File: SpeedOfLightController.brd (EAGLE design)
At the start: 99.7 x 100 mm, 140 parts, among them IC10 74LS595D, IC11 74LS595D, Q10 FDN360P, Q12 FDN360P, Q14 FDN360P, Q16 FDN360P, Q18 FDN360P, Q20 FDN360P, Q22 FDN360P, Q24 FDN360P, Q26 FDN360P, SW2 MOMENTARYBUTTON, U1 ATMEGA328PBTQFP-32, U2 LM380NDIP14, U3 AD5111ADLFCSP10, X1 JST-XH-08-PIN-LONG-PAD, X10 JST-XH-06-PIN-LONG-PAD, X11 JST-XH-06-PIN-LONG-PAD, X12 JST-XH-06-PIN-LONG-PAD, X13 JST-XH-06-PIN-LONG-PAD, X14 JST-XH-07-PIN-LONG-PAD, X15 JST-XH-02-PIN-LONG-PAD, X16 JST-XH-02-PIN-LONG-PAD, X17 JST-XH-02-PIN-LONG-PAD, X18 JST-XH-02-PIN-LONG-PAD, X19 JST-XH-03-PIN-LONG-PAD, X2 JST-XH-08-PIN-LONG-PAD, X20 JST-XH-03-PIN-LONG-PAD, X21 JST-XH-03-PIN-LONG-PAD, X22 JST-XH-03-PIN-LONG-PAD, X3 JST-XH-08-PIN-LONG-PAD, X4 JST-XH-08-PIN-LONG-PAD, X5 JST-XH-08-PIN-LONG-PAD, X6 JST-XH-08-PIN-LONG-PAD, X7 JST-XH-08-PIN-LONG-PAD, X8 JST-XH-08-PIN-LONG-PAD, X9 JST-XH-08-PIN-LONG-PAD

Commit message: USBPD design review
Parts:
- removed CN1: (no value), adafruit:USB-MINIB
- removed F3: FIDUCIAL, ECE388:FIDUCIAL_1MM
- removed IC10, IC11: 74LS595D, 74xx-us:SO16
- removed JP13: (no value), pinhead:1X05
- removed JP14: (no value), pinhead:1X03
- removed R5: 82K, rcl:R0805
- removed SW2: MOMENTARYBUTTON, ECE388:SPST_NO_SMD
- removed X27: (no value), ECE388:W237-102
- added C14, C15: 0.1uF, rcl:C0805
- added C16: 680uF, rcl:140CLH-0810
- added C17: 220uF, rcl:140CLH-0810
- added H1, H2: MOUNT-HOLE3.0, holes:3,0
- added IC1, IC2: 74LS595D, 74xx-us:SO16
- added IC3: (no value), linear:TO263-5
- added J1: 6_PIN_SERIAL_CABLEPTH, SparkFun-Connectors:FTDI_BASIC
- added JP10: (no value), pinhead:1X03
- added JP2: JUMPER-SMT_3_1-NC_TRACE_SILK, SparkFun-Jumpers:SMT-JUMPER_3_1-NC_TRACE_SILK
- added JP5: (no value), pinhead:1X05
- added JP6: (no value), pinhead:1X04
- added JP7, JP8, JP9: (no value), pinhead:1X01
- added R59, R62: 1K5, rcl:R0805
- added R60, R63: 470, rcl:R0805
- added R61: 10K, rcl:R0805
- added SJ1, SJ3: (no value), ECE388:SJ
- added SJ4, SJ5: (no value), jumper:SJ_2W
- added SW1: MOMENTARYBUTTON, ECE388:SPST_NO_SMD
- added U4: AD5141ADLFCSP3, tmc:QFN50P300X300X80-17T160N
- added X25: JST-XH-03-PIN-LONG-PAD, Rembrandt Electronics - JST XH Connectors v1-0:JST-XH-03-PACKAGE-LONG-PAD
- C1, C4: value (none) -> 0.1uF
- C10, C12: value (none) -> 470uF; device rcl:C0805 -> rcl:140CLH-0810
- C11: value (none) -> 47uF
- C13: value (none) -> 4.7uF
- C2, C3: value (none) -> 22pF
- C7: value 22uF -> 0.1uF
- C8: value 22uF -> 47nF
- C9: value (none) -> 47nF
- F1: value (none) -> FIDUCIAL; device adafruit:1812 -> ECE388:FIDUCIAL_1MM
- JP1: value (none) -> JUMPER-SMT_3_1-NC_TRACE_SILK; device pinhead:2X03 -> SparkFun-Jumpers:SMT-JUMPER_3_1-NC_TRACE_SILK
- Q1: value (none) -> 16MHz
- Q10, Q14, Q16, Q20, Q22, Q24, Q26: value FDN360P -> AO3414SOT23; device transistor-power:SUPER-SOT3 -> tmc:SOT95P240X110-3N
- Q11, Q13, Q17, Q19, Q5, Q6, Q7: value (none) -> AO3415; device adafruit:SOT23 -> tmc:SOT95P240X110-3N
- Q12, Q18: value FDN360P -> AO3415; device transistor-power:SUPER-SOT3 -> tmc:SOT95P240X110-3N
- Q15, Q2, Q21, Q23, Q25, Q3, Q4, Q8, Q9: value (none) -> AO3414SOT23; device adafruit:SOT23 -> tmc:SOT95P240X110-3N
- R11, R17, R23, R29, R35, R41, R49, R51, R55: value 1K -> 10K
- R14, R20, R26, R32, R38, R44, R46, R54, R8: value 10K -> 1K
- R57: value 10K -> 0; device rcl:R0805 -> rcl:R0805W
- R6: value 4.3K -> 10K
- SJ2: device jumper:SJ_2 -> jumper:SJ_2W
- U$1: value MT3608SOT23-6 -> USBMICRO; device tmc:SOT95P280X110-6N -> tmc:USBMICRO
- U3: value AD5111ADLFCSP10 -> SSM2305ADMSOP8_2; device tmc:SON50P200X200X80-9T100X160N -> tmc:SOP65P490X95-8N
- X1, X2, X4, X5: value JST-XH-08-PIN-LONG-PAD -> JST-XH-06-PIN-LONG-PAD; device Rembrandt Electronics - JST XH Connectors v1-0:JST-XH-08-PACKAGE-LONG-PAD -> Rembrandt Electronics - JST XH Connectors v1-0:JST-XH-06-PACKAGE-LONG-PAD
- X10, X11, X12, X13: value JST-XH-06-PIN-LONG-PAD -> JST-XH-08-PIN-LONG-PAD; device Rembrandt Electronics - JST XH Connectors v1-0:JST-XH-06-PACKAGE-LONG-PAD -> Rembrandt Electronics - JST XH Connectors v1-0:JST-XH-08-PACKAGE-LONG-PAD
- X14: value JST-XH-07-PIN-LONG-PAD -> JST-XH-08-PIN-LONG-PAD; device Rembrandt Electronics - JST XH Connectors v1-0:JST-XH-07-PACKAGE-LONG-PAD -> Rembrandt Electronics - JST XH Connectors v1-0:JST-XH-08-PACKAGE-LONG-PAD
- X15, X16, X17: value JST-XH-02-PIN-LONG-PAD -> (none); device Rembrandt Electronics - JST XH Connectors v1-0:JST-XH-02-PACKAGE-LONG-PAD -> ECE388:W237-102
- X19, X20, X21: value JST-XH-03-PIN-LONG-PAD -> JST-XH-02-PIN-LONG-PAD; device Rembrandt Electronics - JST XH Connectors v1-0:JST-XH-03-PACKAGE-LONG-PAD -> Rembrandt Electronics - JST XH Connectors v1-0:JST-XH-02-PACKAGE-LONG-PAD
- X23, X24: value (none) -> JST-XH-03-PIN-LONG-PAD; device ECE388:W237-102 -> Rembrandt Electronics - JST XH Connectors v1-0:JST-XH-03-PACKAGE-LONG-PAD
- X3: value JST-XH-08-PIN-LONG-PAD -> JST-XH-07-PIN-LONG-PAD; device Rembrandt Electronics - JST XH Connectors v1-0:JST-XH-08-PACKAGE-LONG-PAD -> Rembrandt Electronics - JST XH Connectors v1-0:JST-XH-07-PACKAGE-LONG-PAD
- moved F1 130.6 mm to (99.1, 130.8)
- moved X11 91.0 mm to (60.3, 118.7), turned to 270 degrees
- moved X10 88.3 mm to (50.2, 118.7), turned to 270 degrees
- moved C7 87.3 mm to (69.2, 90.2), turned to 270 degrees
- moved U2 81.5 mm to (76.2, 59.7), turned to 180 degrees
- moved R3 80.1 mm to (74.3, 93.3), turned to 0 degrees
- moved C9 79.5 mm to (76.2, 65.4), turned to 180 degrees
- moved R21 78.1 mm to (80.0, 99.1)
- moved X13 76.5 mm to (80.6, 118.7), turned to 270 degrees
- moved X12 76.4 mm to (70.5, 118.7), turned to 270 degrees
- moved C10 75.5 mm to (75.6, 43.2), turned to 180 degrees
- moved R55 74.8 mm to (23.5, 87.6), turned to 270 degrees
- moved Q10 74.7 mm to (79.4, 103.5), turned to 90 degrees
- moved R24 73.6 mm to (77.5, 99.1)
- moved R9 73.5 mm to (69.8, 99.1), turned to 90 degrees
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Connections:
- removed net N$26: C11.2, X23.1
- removed net N$33: C7.1, D1.C, F1.1, R5.2
- removed net SOUND_C: R58.1, U1.3, U3.6
- removed net SOUND_UD: U1.22, U3.7
- new net ADSOUND+: SJ4.1, U3.5
- new net ADSOUND-: SJ5.3, U3.8
- new net D+: JP5.3, R58.1, R59.2, R60.2, U$1.P$3
- new net D-: JP5.2, R61.2, R62.1, R63.1, U$1.P$2
- new net FTDIRX: J1.TXO, JP1.2
- new net FTDITX: J1.RXI, JP2.2
- new net LMSOUND: C12.-, SJ4.3
- new net N$40: IC3.5, SJ2.2
- new net N$41: C17.+, IC3.4, L1.P$2, SJ3.2
- new net SOUND+: SJ4.2, X15.1
- new net SOUND-: SJ5.2, X16.2
- new net UCD+: R60.1, U1.6
- new net UCD-: R63.2, U1.3
- net +12V: now also C16.+, IC3.1, JP10.2, Q11.2, Q13.2, Q17.2, Q19.2, Q5.2, Q6.2, Q7.2, R13.2, R14.2, R15.2, R25.2, R26.2, R37.2, R38.2, SJ1.2, SJ2.3, X19.1, X19.2, X20.1, X20.2, X21.1, X21.2; no longer F1.2, JP14.2, Q10.2, Q14.2, Q16.2, Q20.2, Q22.2, Q24.2, Q26.2, R23.2, R31.2, R35.2, R43.2, R47.2, R51.2, R55.2, X15.1, X15.2, X16.1, X16.2, X17.2, X27.1
- net +5V: now also C10.+, C14.2, C15.1, C4.2, C6.1, C7.1, IC1.16, IC2.16, J1.VCC, JP10.1, R4.2, R6.2, R61.1, SJ3.1, U3.6, U4.10, U4.13, U4.16, U4.9, X3.1; no longer C1.1, C12.2, C2.1, C8.1, C9.1, CN1.VBUS, IC10.16, IC11.16, JP1.5, JP13.1, JP14.1, L1.P$1, R3.2, R57.2, SJ2.3, U$1.5, X14.1
- net A: now also Q20.3, X10.5, X11.5, X12.5, X13.5, X14.5; no longer Q4.3, X1.5, X2.5, X3.5, X4.5, X5.5
- net AN1: now also IC1.7, R7.1; no longer IC10.7, R21.1
- net AN2: now also IC2.15, R19.1; no longer IC11.15, R25.1
- net AN3: now also IC2.1, R31.1; no longer IC11.1, R29.1
- net AN4: now also IC2.2, R8.1; no longer IC11.2, R33.1
- net AN5: now also IC2.3, R20.1; no longer IC11.3, R37.1
- net AN6: now also IC2.4, R32.1; no longer IC11.4, R41.1
- net AN7: now also IC2.5, R9.1; no longer IC11.5, R45.1
- net AN8: now also IC2.6, R21.1; no longer IC11.6, R49.1
- net AN9: now also IC2.7, R33.1; no longer IC11.7, R53.1
- net B: now also Q21.3, X10.6, X11.6, X12.6, X13.6, X14.6; no longer Q2.3, X1.6, X2.6, X3.6, X4.6, X5.6
- net B_COL_0: now also X1.4, X2.4; no longer X10.4, X11.4
- net B_COL_1: now also X1.5, X2.5; no longer X10.5, X11.5
- net B_COL_2: now also X1.6, X2.6; no longer X10.6, X11.6
- net B_COL_3: now also X4.4, X5.4; no longer X12.4, X13.4
- net B_COL_4: now also X4.5, X5.5; no longer X12.5, X13.5
- net B_COL_5: now also X4.6, X5.6; no longer X12.6, X13.6
- net B_ROW_0: now also X1.1, X4.1; no longer X10.1, X12.1
- net B_ROW_1: now also X1.2, X4.2; no longer X10.2, X12.2
- net B_ROW_2: now also X1.3, X4.3; no longer X10.3, X12.3
- net B_ROW_3: now also X2.1, X5.1; no longer X11.1, X13.1
- net B_ROW_4: now also X2.2, X5.2; no longer X11.2, X13.2
- net B_ROW_5: now also X2.3, X5.3; no longer X11.3, X13.3
- net C: now also Q22.3, X10.7, X11.7, X12.7, X13.7, X14.7; no longer Q3.3, X1.7, X2.7, X3.7, X4.7, X5.7
- net D: now also Q23.3, X10.1, X11.1, X12.1, X13.1, X14.1; no longer Q5.3, X1.1, X2.1, X3.1, X4.1, X5.1
- net DTR: now also C1.2, J1.DTR; no longer C6.2, JP1.6
- net E: now also Q24.3, X10.2, X11.2, X12.2, X13.2, X14.2; no longer Q6.3, X1.2, X2.2, X3.2, X4.2, X5.2
- net F: now also Q25.3, X10.4, X11.4, X12.4, X13.4, X14.4; no longer Q7.3, X1.4, X2.4, X3.4, X4.4, X5.4
- net G: now also Q26.3, X10.3, X11.3, X12.3, X13.3, X14.3; no longer Q8.3, X1.3, X2.3, X3.3, X4.3, X5.3
- net GND: now also C10.-, C11.2, C14.1, C15.2, C16.-, C17.-, C2.1, C6.2, C9.1, D1.A, IC1.8, IC2.8, IC3.3, IC3.6, J1.CTS, J1.GND, JP10.3, JP5.5, JP6.1, JP6.2, JP6.3, JP6.4, JP7.1, JP8.1, JP9.1, Q10.2, Q14.2, Q16.2, Q20.2, Q22.2, Q24.2, Q26.2, R11.1, R17.1, R23.1, R29.1, R3.1, R35.1, R41.1, R49.1, R51.1, R55.1, R57.1, R59.1, R62.2, SJ5.1, SW1.1, U$1.P$5, U$1.P$6, U$1.P$8, U3.7, U4.1, U4.15, U4.17, U4.5, U4.7, U4.8, X17.2, X23.1, X23.2, X23.3, X24.1, X24.3, X25.1, X25.2, X25.3, X3.7; no longer C1.2, C10.2, C12.1, C2.2, C8.2, C9.2, CN1.GND, IC10.8, IC11.8, JP1.1, JP1.3, JP13.5, JP14.3, Q11.2, Q13.2, Q17.2, Q19.2, Q5.2, Q6.2, Q7.2, R14.1, R20.1, R26.1, R32.1, R38.1, R4.1, R44.1, R46.1, R54.1, R6.1, R8.1, SW2.1, U$1.2, U3.4, U3.5, X14.7, X19.1, X19.2, X19.3, X20.1, X20.2, X20.3, X21.1, X21.2, X21.3, X27.2
- net LED_B: now also IC1.10, IC2.10, X3.5; no longer IC10.10, IC11.10, X14.5
- net LED_D_OUT: now also IC2.9, X3.2; no longer IC11.9, X14.2
- net LED_L: now also IC1.12, IC2.12, X3.4; no longer IC10.12, IC11.12, X14.4
- net LED_O: now also IC1.13, IC2.13, R3.2, X3.6; no longer IC10.13, IC11.13, R4.2, X14.6
- net MISO: now also U4.14
- net MOSI: now also IC1.14, U4.12; no longer IC10.14
- net N$1: now also Q21.1, R44.2, R49.2; no longer Q2.1, R7.2, R8.2
- net N$10: now also Q14.1, R31.2, R34.2; no longer Q13.1, R29.2, R30.2
- net N$11: now also Q3.1, R11.2, R8.2; no longer Q15.1, R33.2, R34.2
- net N$12: now also Q9.1, R20.2, R23.2; no longer Q17.1, R37.2, R38.2
- net N$13: now also Q15.1, R32.2, R35.2; no longer Q19.1, R41.2, R42.2
- net N$14: now also Q4.1, R12.2, R9.2; no longer Q21.1, R45.2, R46.2
- net N$15: now also Q10.1, R21.2, R24.2; no longer Q23.1, R49.2, R50.2
- net N$16: now also Q16.1, R33.2, R36.2; no longer Q25.1, R53.2, R54.2
- net N$17: now also C2.2; no longer C3.2
- net N$18: now also C3.2; no longer C4.2
- net N$19: now also JP5.1, SJ1.1, U$1.P$1; no longer R5.1, R6.2, U$1.3
- net N$2: now also Q22.1, R45.2, R50.2; no longer Q3.1, R10.2, R9.2
- net N$20: now also X15.2, X16.1; no longer X23.2, X24.1
- net N$21: now also C12.+, U2.8; no longer CN1.D+, JP13.2
- net N$22: now also C11.1; no longer C10.1
- net N$23: now also C9.2, U3.4; no longer CN1.D-, JP13.3
- net N$24: now also C8.2, U3.3; no longer D1.A, L1.P$2, U$1.1
- net N$25: now also R57.2, U4.4; no longer C11.1, U2.8
- net N$27: now also Q16.3, Q19.1, R39.1; no longer Q25.3, Q26.1, R55.1
- net N$28: now also Q10.3, Q13.1, R27.1; no longer Q23.3, Q24.1, R51.1
- net N$29: now also Q4.3, Q7.1, R15.1; no longer Q21.3, Q22.1, R47.1
- net N$3: now also Q23.1, R46.2, R51.2; no longer Q5.1, R11.2, R12.2
- net N$30: now also Q3.3, Q6.1, R14.1; no longer Q15.3, Q16.1, R35.1
- net N$31: now also JP5.4, U$1.P$4; no longer CN1.ID, JP13.4
- net N$32: now also D1.C, IC3.2, L1.P$1; no longer SJ2.2, U$1.4
- net N$34: now also Q12.1, Q9.3, R26.1; no longer Q17.3, Q18.1, R39.1
- net N$35: now also Q15.3, Q18.1, R38.1; no longer Q19.3, Q20.1, R43.1
- net N$36: now also Q14.3, Q17.1, R37.1; no longer Q13.3, Q14.1, R31.1
- net N$37: now also Q11.1, Q8.3, R25.1; no longer Q11.3, Q12.1, R27.1
- net N$38: now also Q2.3, Q5.1, R13.1; no longer Q10.1, Q9.3, R23.1
- net N$39: now also IC1.9, IC2.14; no longer IC10.9, IC11.14
- net N$4: now also Q24.1, R47.2, R52.2; no longer Q6.1, R15.2, R16.2
- net N$5: now also Q20.1, R43.2, R48.2; no longer Q4.1, R13.2, R14.2
- net N$6: now also Q25.1, R53.2, R55.2; no longer Q7.1, R17.2, R18.2
- net N$7: now also Q26.1, R54.2, R56.2; no longer Q8.1, R19.2, R20.2
- net N$8: now also Q2.1, R10.2, R7.2; no longer Q9.1, R21.2, R22.2
- net N$9: now also Q8.1, R19.2, R22.2; no longer Q11.1, R25.2, R26.2
- net RX: now also JP1.3, JP2.1; no longer JP1.2
- net SCK: now also IC1.11, IC2.11, U4.11, X3.3; no longer IC10.11, IC11.11, X14.3
- net SCORE0_1: now also Q5.3, R16.2, X6.8; no longer Q10.3, R24.2, X1.8
- net SCORE0_10: now also Q11.3, X7.8; no longer Q12.3, X2.8
- net SCORE0_100: now also Q17.3, R40.2, X8.8; no longer Q14.3, R32.2, X3.8
- net SCORE1_1: now also Q6.3, R17.2, X9.8; no longer Q16.3, R36.2, X4.8
- net SCORE1_10: now also Q12.3, R29.2, X10.8; no longer Q18.3, R40.2, X5.8
- net SCORE1_100: now also Q18.3, R41.2, X11.8; no longer Q20.3, R44.2, X6.8
- net SCORE2_1: now also Q7.3, R18.2, X12.8; no longer Q22.3, R48.2, X7.8
- net SCORE2_10: now also Q13.3, R30.2, X13.8; no longer Q24.3, R52.2, X8.8
- net SCORE2_100: now also Q19.3, R42.2, X14.8; no longer Q26.3, R56.2, X9.8
- net SIGA: now also IC1.15, R43.1; no longer IC10.15, R13.1
- net SIGB: now also IC1.1, R44.1; no longer IC10.1, R7.1
- net SIGC: now also IC1.2, R45.1; no longer IC10.2, R9.1
- net SIGD: now also IC1.3, R46.1; no longer IC10.3, R11.1
- net SIGE: now also IC1.4, R47.1; no longer IC10.4, R15.1
- net SIGF: now also IC1.5, R53.1; no longer IC10.5, R17.1
- net SIGG: now also IC1.6, R54.1; no longer IC10.6, R19.1
- net SOUNDOUT: now also U4.2; no longer U3.2
- net SOUND_ATND: now also C8.1, U4.3; no longer U3.3
- net SOUND_CS: now also R4.1, U1.22, U4.6; no longer R57.1, U1.6, U3.8
- net TX: now also JP1.1, JP2.3; no longer JP1.4
- net UC_RESET: now also C1.1, R6.1, SW1.3; no longer C6.1, R3.1, SW2.3
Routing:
- net +12V: track 283.9 -> 381.0 mm, vias 0 -> 4
- net +5V: track 166.4 -> 261.0 mm, vias 8 -> 13
- net SOUND_UD: track 83.4 -> 0.00 mm, vias 11 -> 0
- net SOUND_C: track 67.2 -> 0.00 mm, vias 6 -> 0
- net SOUND_CS: track 70.6 -> 26.2 mm, vias 6 -> 2
- net UCD-: track 0.00 -> 38.0 mm
- net N$25: track 35.7 -> 2.05 mm
- net UCD+: track 0.00 -> 33.5 mm
- net N$41: track 0.00 -> 33.4 mm
- net GND: track 102.5 -> 135.3 mm, vias 71 -> 148
- net SOUNDOUT: track 47.4 -> 15.3 mm, vias 4 -> 0
- net N$40: track 0.00 -> 27.5 mm
- net B_COL_2: track 57.4 -> 83.6 mm, vias 0 -> 4
- net B_ROW_0: track 28.2 -> 53.2 mm, vias 2 -> 0
- net B_ROW_3: track 69.0 -> 44.5 mm, vias 4 -> 0
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- removed copper zone on layer 1, net +5V
- removed copper zone on layer 1, net N$24
- removed copper zone on layer 1, net N$33
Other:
- board size 99.7 x 100 mm -> 101 x 132.7 mm
- board text added: "+"
- board text added: "12 GND"
- board text added: "Buttion Board Power"
- board text added: "EN"
- board text added: "FTDI Header"
- board text added: "RESET"
- board text added: "S1"
- board text added: "S2"
- board text removed: "+12V G"
- board text removed: "5"
- board text removed: "Button Board Power"
- board text removed: "C"
- board text removed: "D"
- board text removed: "G"
- board text removed: "R"
- board text removed: "SP + -"
- board text removed: "T"

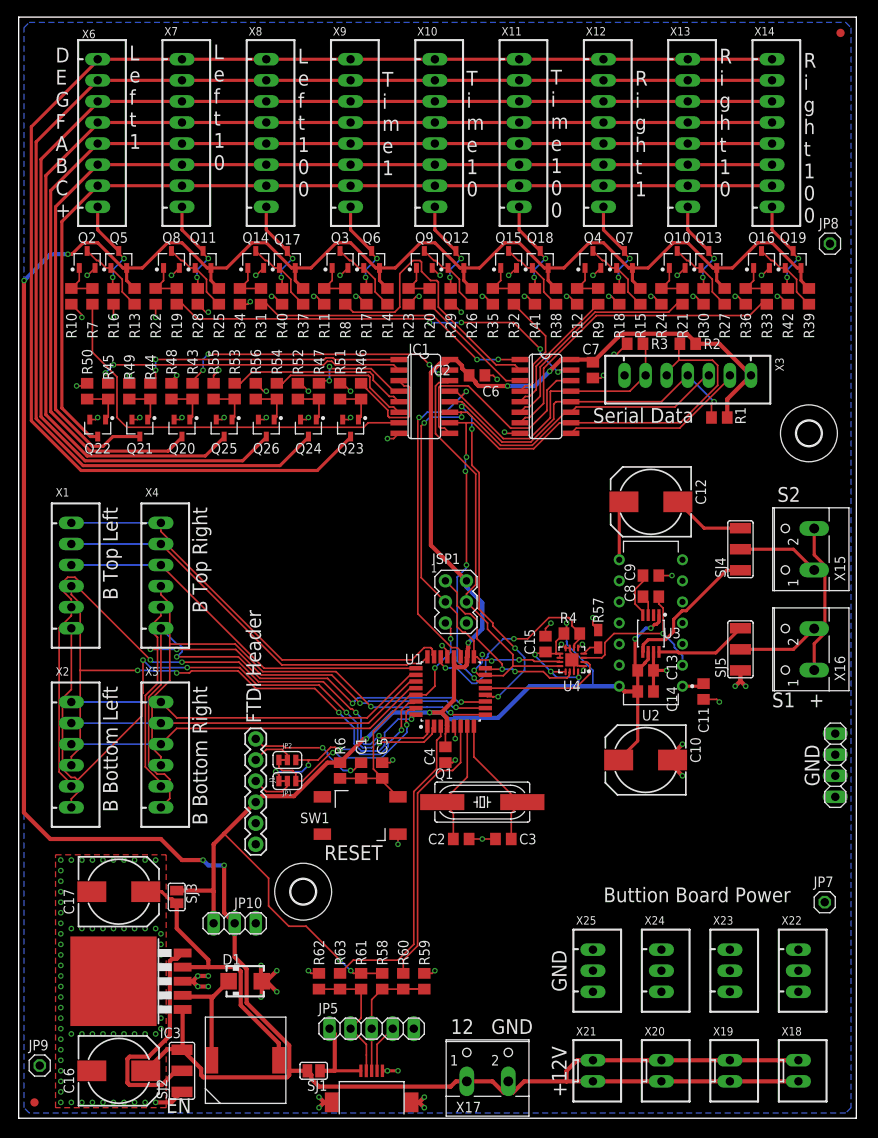
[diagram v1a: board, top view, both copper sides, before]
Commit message: Change to 100mm square board
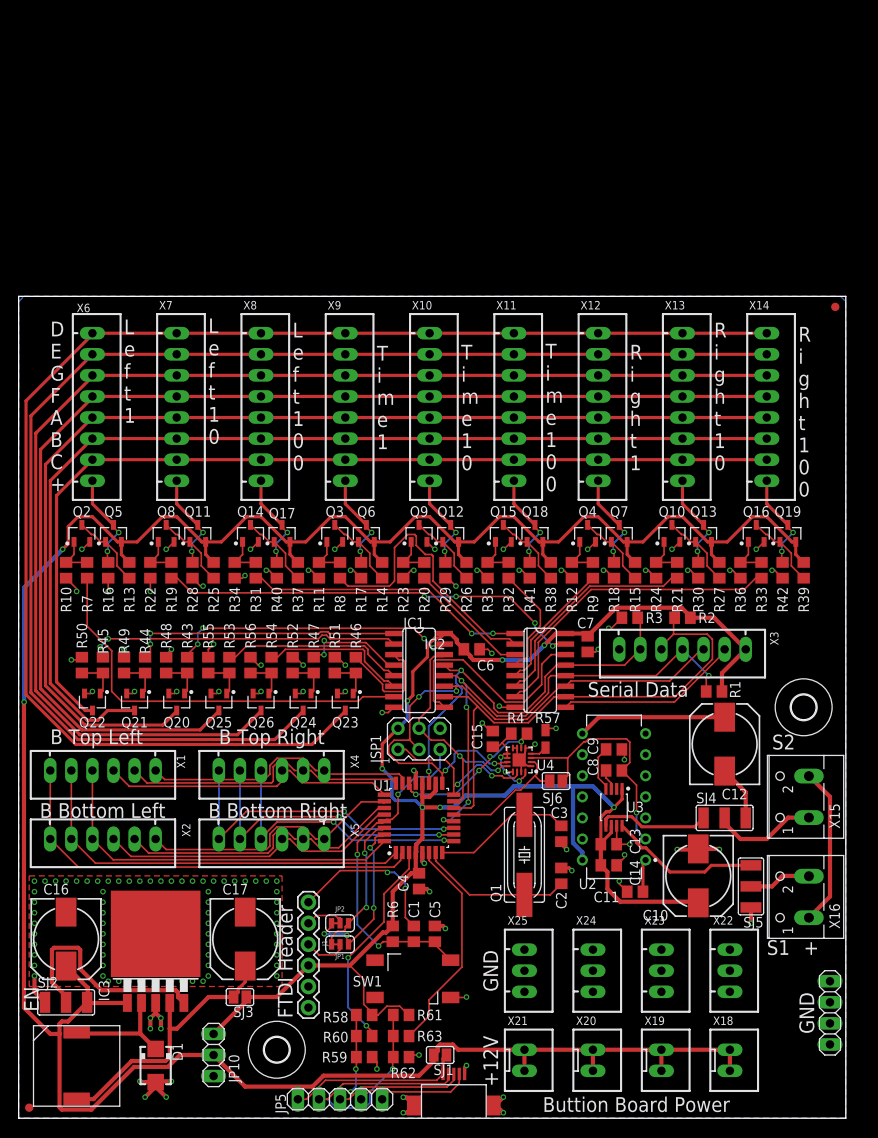
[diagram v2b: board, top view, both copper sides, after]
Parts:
- removed JP7, JP8, JP9: (no value), pinhead:1X01
- removed X17: (no value), ECE388:W237-102
- added SJ6: (no value), ECE388:SJ
- moved X10 33.0 mm to (49.5, 85.7)
- moved X11 33.0 mm to (59.7, 85.7)
- moved X12 33.0 mm to (69.8, 85.7)
- moved X13 33.0 mm to (80.0, 85.7)
- moved X14 33.0 mm to (90.2, 85.7)
- moved X6 33.0 mm to (8.89, 85.7)
- moved X7 33.0 mm to (19.1, 85.7)
- moved X8 33.0 mm to (29.2, 85.7)
- moved X9 33.0 mm to (39.4, 85.7)
- moved C7 33.0 mm to (68.6, 57.1)
- moved IC1 33.0 mm to (48.3, 54.0)
- moved IC2 33.0 mm to (62.9, 54.0)
- moved Q20 33.0 mm to (19.1, 50.2)
- moved Q21 33.0 mm to (14.0, 50.2)
- moved Q22 33.0 mm to (8.89, 50.2)
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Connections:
- net +12V: no longer X17.1
- net GND: no longer JP7.1, JP8.1, JP9.1, X17.2
- net SOUNDOUT: now also SJ6.2
- net SOUND_ATND: now also SJ6.1
- net UCD+: now also U1.3; no longer U1.6
- net UCD-: now also U1.6; no longer U1.3
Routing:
- net +12V: track 381.0 -> 324.5 mm, vias 4 -> 2
- net +5V: track 261.0 -> 218.0 mm, vias 13 -> 10
- net B_COL_1: track 82.7 -> 49.1 mm, vias 4 -> 0
- net B_COL_4: track 68.1 -> 36.1 mm, vias 4 -> 2
- net B_COL_3: track 64.9 -> 33.4 mm
- net B_COL_2: track 83.6 -> 53.2 mm, vias 4 -> 0
- net B_COL_5: track 69.2 -> 38.9 mm, vias 3 -> 2
- net B_COL_0: track 71.0 -> 45.4 mm, vias 4 -> 0
- net LED_O: track 74.2 -> 50.3 mm
- net MOSI: track 53.9 -> 30.2 mm
- net LED_L: track 83.1 -> 61.7 mm
- net D-: track 16.2 -> 35.9 mm, vias 0 -> 1
- net B_ROW_0: track 53.2 -> 33.5 mm
- net LED_B: track 82.3 -> 63.2 mm, vias 4 -> 0
- net B_ROW_1: track 49.4 -> 35.3 mm
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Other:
- board size 101 x 132.7 mm -> 99.7 x 99.1 mm
- board text removed: "12 GND"
- board text removed: "RESET"

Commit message: Board Redone with notes from Ben
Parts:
- removed SW1: MOMENTARYBUTTON, ECE388:SPST_NO_SMD
- added RESET: MOMENTARYBUTTON, ECE388:SPST_NO_SMD
- SJ4, SJ5: device jumper:SJ_2W -> jumper:SJ_2
- moved JP6 54.6 mm to (97.8, 67.3)
- moved R59 18.4 mm to (59.9, 9.27), turned to 270 degrees
- moved R60 15.8 mm to (57.4, 9.27), turned to 270 degrees
- moved R58 13.6 mm to (54.9, 9.27), turned to 90 degrees
- moved SJ1 11.6 mm to (39.4, 5.71)
- moved L1 11.4 mm to (18.4, 6.35), turned to 90 degrees
- moved X18 9.09 mm to (94.6, 5.08)
- moved X19 9.09 mm to (86.4, 5.08)
- moved X20 9.09 mm to (78.1, 5.08)
- moved X22 9.09 mm to (94.6, 15.9)
- moved X23 9.09 mm to (86.4, 15.9)
- moved X24 9.09 mm to (78.1, 15.9)
- moved X25 9.09 mm to (69.8, 15.9)
- moved X21 9.09 mm to (69.8, 5.08)
- moved J1 8.35 mm to (43.2, 27.3)
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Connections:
- net GND: now also RESET.1; no longer SW1.1
- net LED_B: now also U1.22; no longer U1.14
- net SOUND_CS: now also U1.14; no longer U1.22
- net UCD+: now also U1.6; no longer U1.3
- net UCD-: now also U1.3; no longer U1.6
- net UC_RESET: now also RESET.3; no longer SW1.3
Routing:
- net +12V: track 324.5 -> 232.9 mm, vias 2 -> 22
- net +5V: track 218.0 -> 253.9 mm, vias 10 -> 21
- net UC_RESET: track 40.8 -> 66.1 mm, vias 3 -> 5
- net D-: track 35.9 -> 25.2 mm, vias 1 -> 0
- net DTR: track 19.5 -> 8.91 mm, vias 2 -> 0
- net GND: track 134.0 -> 144.3 mm, vias 146 -> 131
- net MOSI: track 30.2 -> 40.2 mm, vias 2 -> 4
- net N$41: track 33.4 -> 23.7 mm
- net N$39: track 28.3 -> 20.0 mm, vias 0 -> 2
- net N$40: track 27.5 -> 19.4 mm, vias 0 -> 2
- net SCK: track 71.7 -> 65.4 mm, vias 4 -> 0
- net TX: track 21.4 -> 15.4 mm, vias 4 -> 2
- net AN4: track 34.3 -> 28.5 mm, vias 0 -> 2
- net LED_B: track 63.2 -> 68.3 mm, vias 0 -> 4
- net AN5: track 14.7 -> 19.3 mm, vias 0 -> 2
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- added copper zone on layer 1, net +12V
- added copper zone on layer 16, net +12V
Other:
- board text added: "- +"
- board text added: "Tim Chase Julia Sorrentino Brad Piva Josh Steakelum Fall 2019 Speed Of Light Controller github.com/timChase98/SpeedOfLightContoller"
- board text removed: "+12V"
